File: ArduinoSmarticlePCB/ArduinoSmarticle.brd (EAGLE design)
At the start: 49.5 x 18.2 mm, 22 parts, among them U1 LSM6DS3DOT_INDICATION

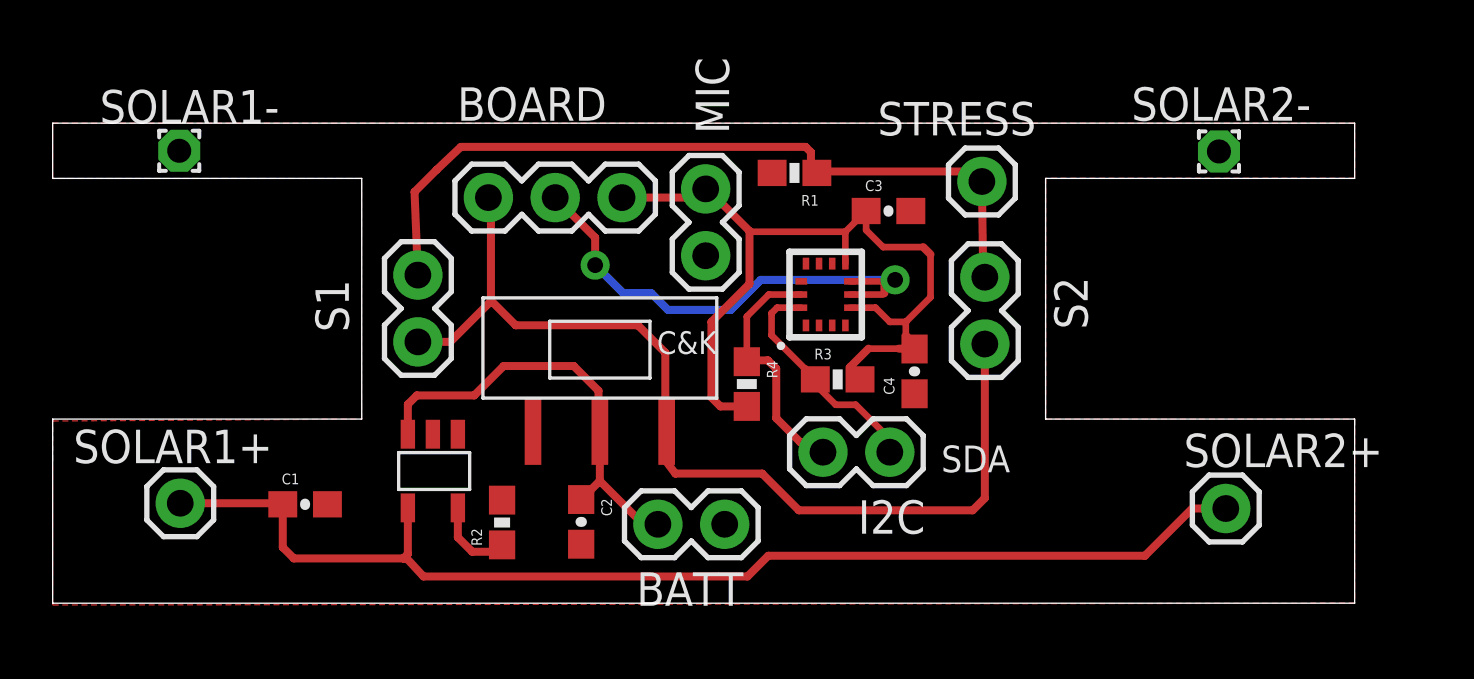
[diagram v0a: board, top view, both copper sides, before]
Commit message: improved size of board and isolation size, added mathematica notebook describing solar panels
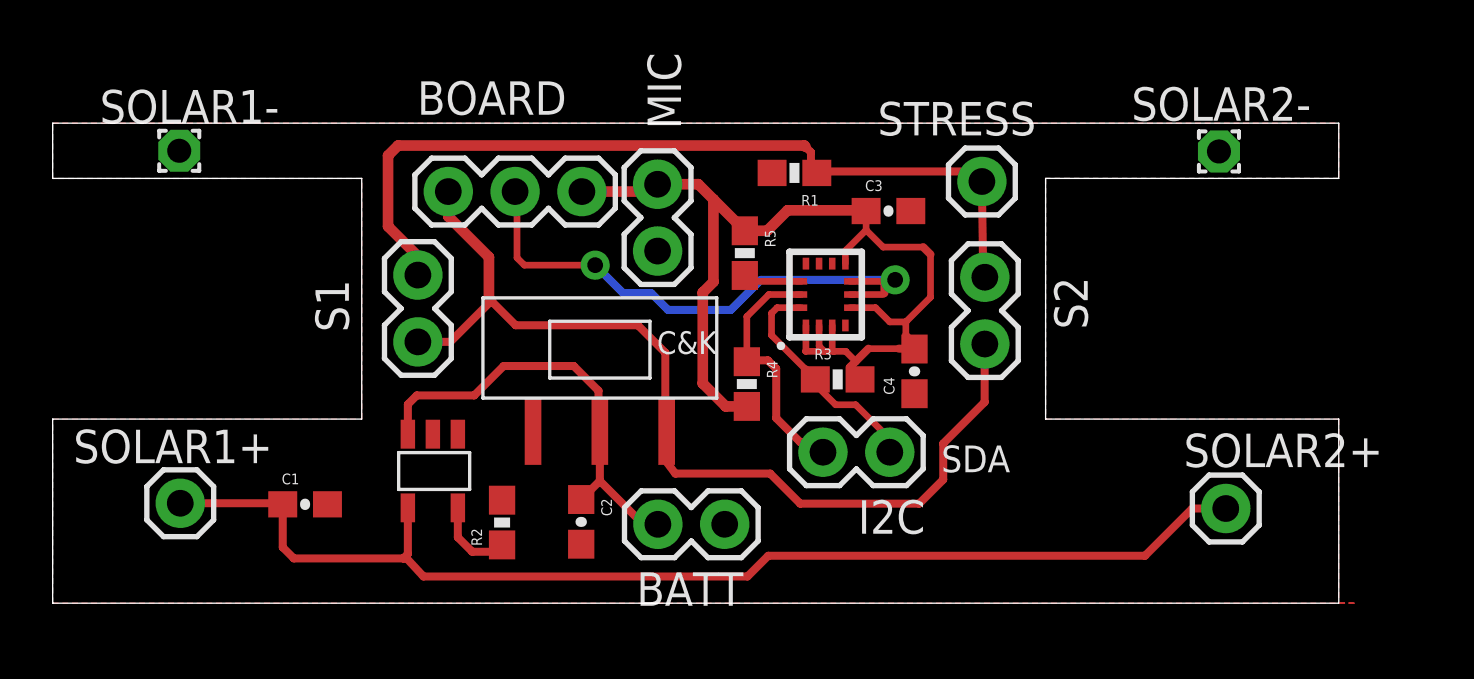
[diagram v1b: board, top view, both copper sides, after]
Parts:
- added R5: 10k, SparkFun-Resistors:0603-RES
- moved MIC 1.84 mm to (23.0, 15.9)
- moved BOARD 1.54 mm to (20.1, 15.6)
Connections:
- new net N$2: R5.2, U1.12
- net VCC: now also R5.1, U1.1, U1.2, U1.3
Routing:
- net VCC: track 34.3 -> 42.2 mm
- net GND: track 19.2 -> 21.7 mm
- net SERVOGND: track 30.0 -> 32.3 mm
- net N$2: track 0.00 -> 2.24 mm
- net V_BATT: track 38.1 -> 37.4 mm
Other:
- board size 49.5 x 18.2 mm -> 48.9 x 18.2 mm
